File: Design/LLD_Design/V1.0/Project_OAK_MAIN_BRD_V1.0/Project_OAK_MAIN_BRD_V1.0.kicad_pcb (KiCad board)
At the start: 4 copper layers, 41.8 x 46 mm, 109 parts, among them U1 ATmega328PB-MU, U2 RV-8263-C7-32.768KHZ-20PPM-TA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, U3 LIS2DW12TR

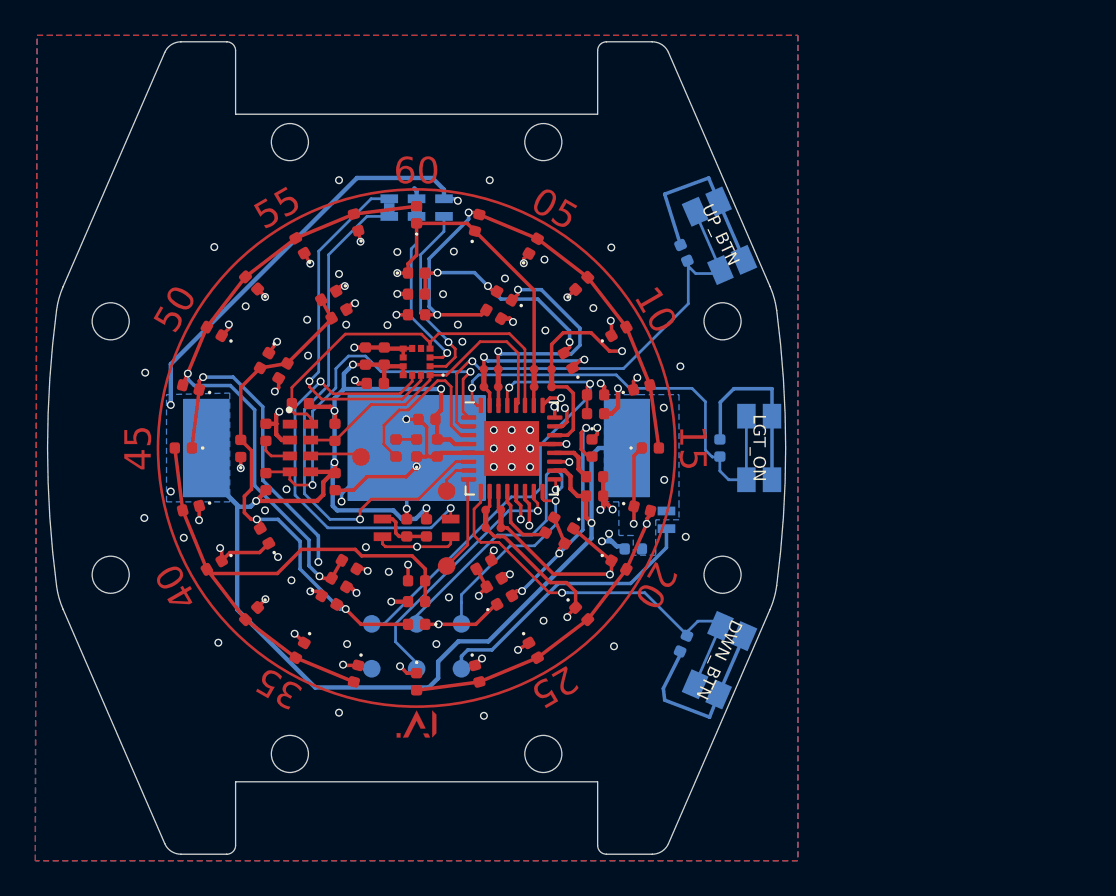
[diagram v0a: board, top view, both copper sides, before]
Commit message: SCH update in progress with ACCL sensor change & haptic sensor addition
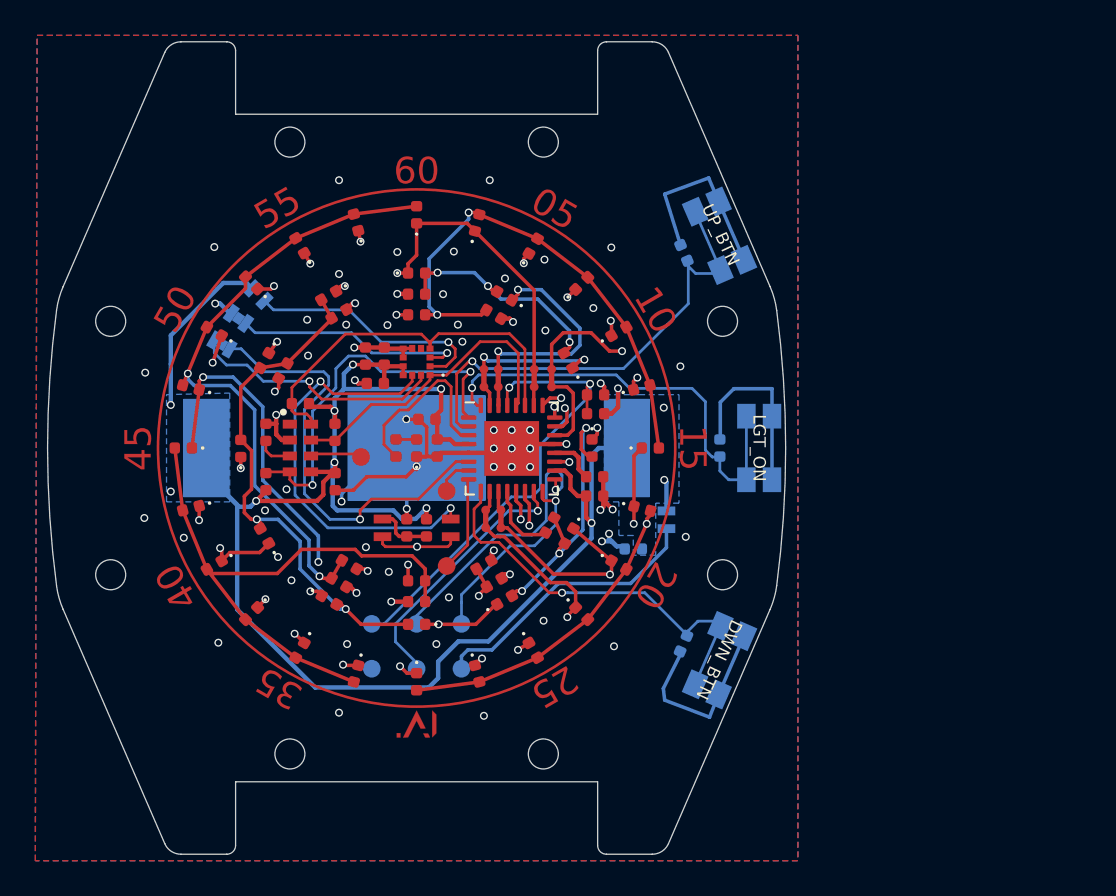
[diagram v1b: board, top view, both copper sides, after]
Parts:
- REF** (x8): footprint MountingHole:MountingHole_2.1mm -> MountingHole:MountingHole_1.7mm
- moved JP5 12.2 mm to (59.4, 87.6), turned to 150 degrees
- moved JP2 11.9 mm to (60.4, 86.1), turned to 325 degrees
- moved JP1 11.6 mm to (61.5, 84.8), turned to 315 degrees
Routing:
- net +3V0: track 123.4 -> 111.4 mm, vias 13 -> 12
- net /ACC_INT1: track 20.5 -> 14.4 mm
- net /PE1: track 30.0 -> 25.0 mm
- net /ACC_SDA0: track 9.78 -> 13.2 mm
- net /ACC_CS: track 11.0 -> 14.1 mm
- net /R5: track 88.5 -> 86.7 mm
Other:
- board text added: "Haptic Sensor"

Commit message: layout update in progress
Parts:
- removed JP1: SolderJumper_2_Open, Jumper:SolderJumper-2_Open_Pad1.0x1.5mm_custom
- removed JP2: SolderJumper_2_Bridged, Jumper:SolderJumper-2_Bridged_Pad1.0x1.5mm_custom
- removed R18, R19, R22, R23, R26: 560E, Resistor_SMD:R_0402_1005Metric
- added C20: 1u, Capacitor_SMD:C_0402_1005Metric, F.Cu at (103.5, 88.1)
- added NT7: Net-Tie_2, NetTie:NetTie-2_SMD_Custom, F.Cu at (61.9, 92.5)
- added R1: 1k, Resistor_SMD:R_0402_1005Metric, F.Cu at (100.8, 90.1)
- added R2: 1k, Resistor_SMD:R_0402_1005Metric, F.Cu at (102.5, 88.1)
- added R3: 100k, Resistor_SMD:R_0402_1005Metric, F.Cu at (101.4, 88.1)
- added R4: 560E, Resistor_SMD:R_0402_1005Metric, F.Cu at (78.1, 97.9)
- added R5: 560E, Resistor_SMD:R_0402_1005Metric, F.Cu at (62.8, 89.1)
- added R8: 560E, Resistor_SMD:R_0402_1005Metric, F.Cu at (74.3, 100.1)
- added R9: 560E, Resistor_SMD:R_0402_1005Metric, F.Cu at (70.5, 101.0)
- added TP2: TestPoint, TestPoint:TestPoint_Pad_D1.0mm, B.Cu at (98.2, 85.7)
- added TP8: TestPoint, TestPoint:TestPoint_Pad_D1.0mm, B.Cu at (98.2, 88.8)
- added U4: DRV2605LYZF, Sensor:DRV2605LYZFR, F.Cu at (102.4, 90.2)
- C11: value 10u -> 1u
- R10, R11: value 10k -> 4.7k
- R7: value 10k -> 560E
- U3: value LIS2DW12TR -> BMA400; footprint Sensor:LIS2DW12TR -> Sensor:BMA400
- moved C11 36.5 mm to (104.0, 90.1)
- moved R7 10.8 mm to (70.5, 85.9), turned to 0 degrees
- moved C10 4.92 mm to (72.4, 87.3), turned to 90 degrees
- moved C5 0.38 mm to (68.6, 87.9), turned to 270 degrees
- moved U3 0.38 mm to (70.5, 88.2)
- moved R13 0.06 mm to (66.6, 100.1)
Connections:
- net /C1_T renamed /LED MATRIX/C1_T
- net /C2_T renamed /LED MATRIX/C2_T
- net /C4_T renamed /LED MATRIX/C4_T
- net /C5_T renamed /LED MATRIX/C5_T
- net /C6_T renamed /LED MATRIX/C6_T
- C16 pad 1: /C3_T -> /LED MATRIX/C3_T
- D10 pad 2: /C3_T -> /LED MATRIX/C3_T
- D16 pad 2: /C3_T -> /LED MATRIX/C3_T
- D22 pad 2: /C3_T -> /LED MATRIX/C3_T
- D28 pad 2: /C3_T -> /LED MATRIX/C3_T
- D34 pad 2: /C3_T -> /LED MATRIX/C3_T
- D4 pad 2: /C3_T -> /LED MATRIX/C3_T
- R7 pad 1: /RTC_CLKO_EN -> /C3
- R7 pad 2: GND -> /LED MATRIX/C3_T
- U3 pad 1: /SNS_SCL -> GND
- U3 pad 11: /ACC_INT2 -> (no net)
- U3 pad 12: /ACC_INT1 -> /SNS_SCL
- U3 pad 2: /ACC_CS -> /SNS_SDA
- U3 pad 3: /ACC_SDA0 -> +3V0
- U3 pad 4: /SNS_SDA -> (no net)
- U3 pad 5: (no net) -> /ACC_INT1
- U3 pad 6: GND -> /ACC_INT2
- U3 pad 7: GND -> +3V0
- U3 pad 9: +3V0 -> GND
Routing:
- net /C3_T: track 29.0 -> 0.00 mm, vias 2 -> 1
- net /LED MATRIX/C3_T: track 0.00 -> 28.0 mm, vias 0 -> 1
- net /ACC_CS: track 14.1 -> 0.00 mm, vias 1 -> 0
- net /ACC_SDA0: track 13.2 -> 0.00 mm, vias 1 -> 0
- net +3V0: track 111.4 -> 104.5 mm
- net /SNS_SCL: track 17.5 -> 13.3 mm
- net GND: track 82.9 -> 78.8 mm, vias 66 -> 61
- net /SNS_SDA: track 22.2 -> 18.4 mm
- net /MON_LED: track 10.5 -> 7.68 mm
- net /ACC_INT2: track 23.8 -> 25.2 mm
- net /RTC_INTO: track 21.6 -> 22.8 mm
- net /ACC_INT1: track 14.4 -> 15.5 mm

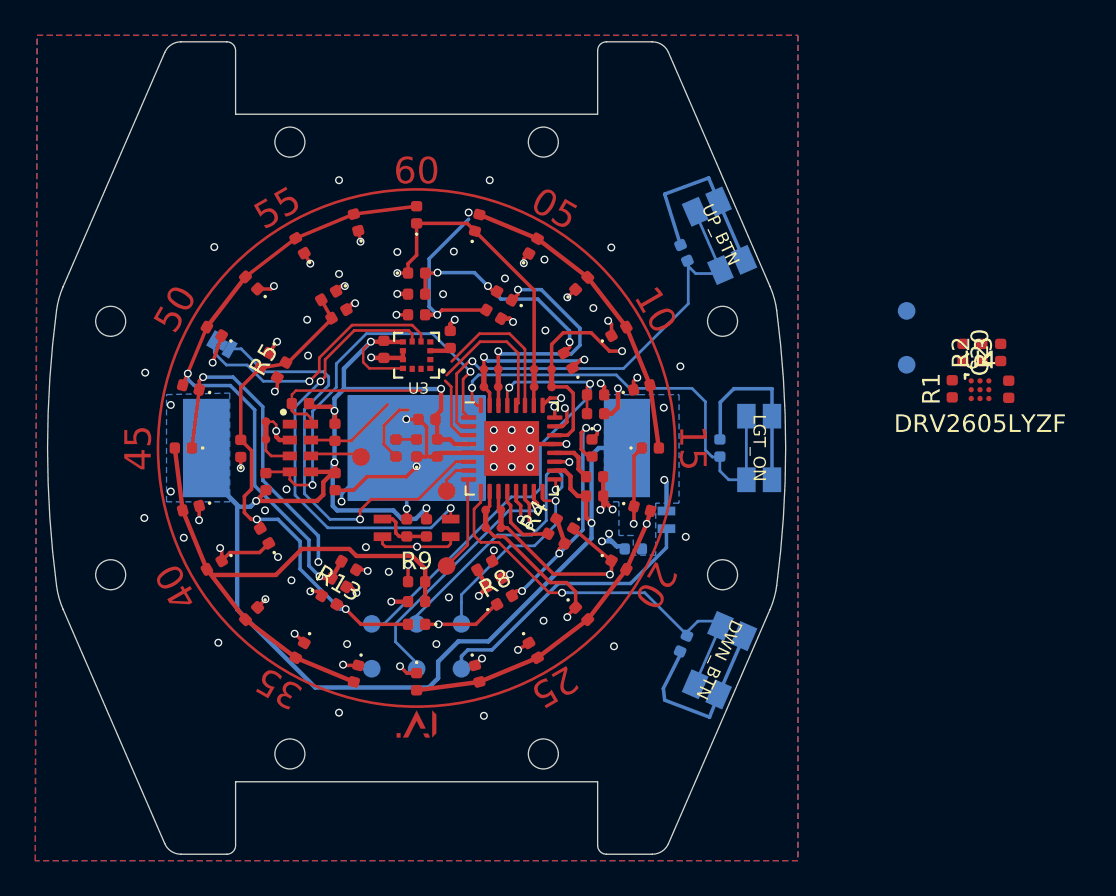
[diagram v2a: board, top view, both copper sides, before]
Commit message: OAK V1.0 main board layout update
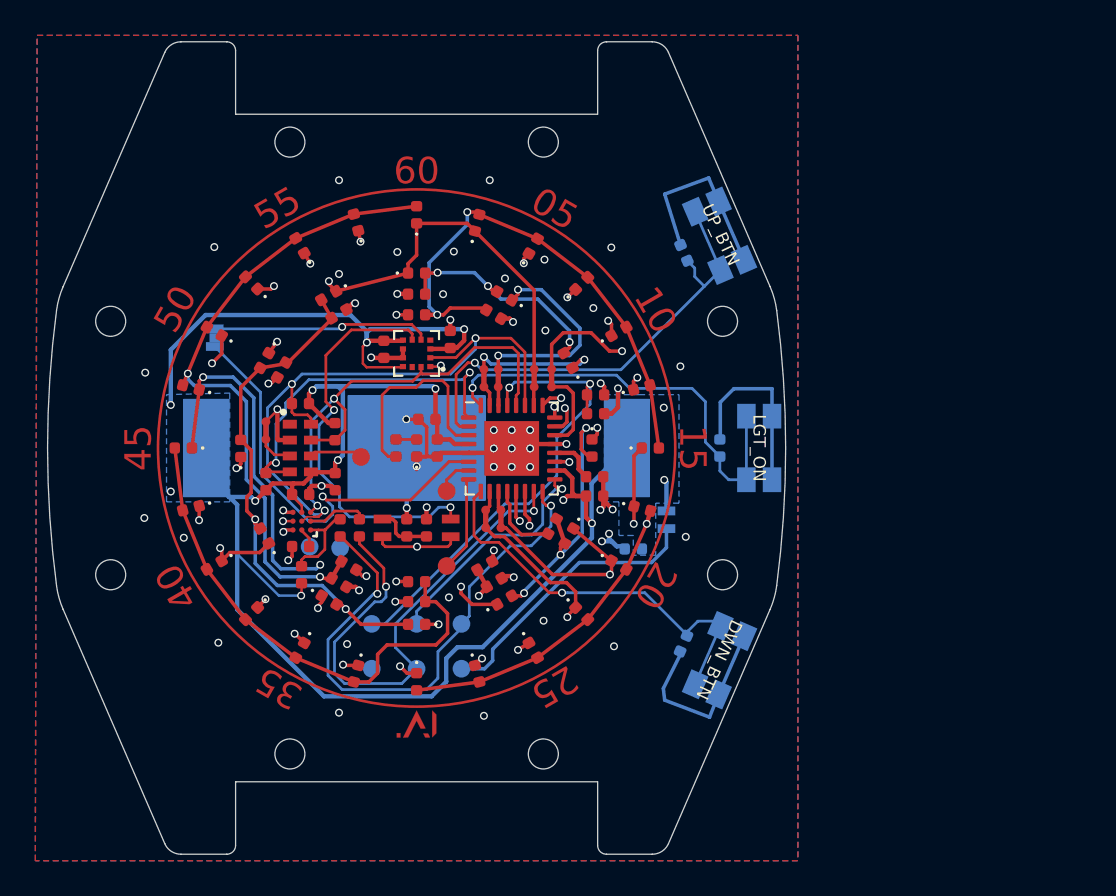
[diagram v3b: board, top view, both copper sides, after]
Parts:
- moved C20 41.1 mm to (63.9, 99.0), turned to 180 degrees
- moved C11 40.5 mm to (63.9, 96.1), turned to 0 degrees
- moved R3 39.5 mm to (63.9, 100.6), turned to 90 degrees
- moved U4 39.1 mm to (64.0, 97.6), turned to 180 degrees
- moved R2 37.7 mm to (66.1, 98.0), turned to 270 degrees
- moved TP8 35.3 mm to (64.4, 99.1)
- moved TP2 34.8 mm to (66.1, 99.1)
- moved R1 34.5 mm to (67.2, 98.0), turned to 270 degrees
- moved JP5 0.56 mm to (59.0, 87.2), turned to 90 degrees
- moved U3 0.10 mm to (70.5, 88.1)
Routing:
- net +3V0: track 104.5 -> 134.0 mm, vias 12 -> 15
- net /ICSP_MISO: track 11.2 -> 31.1 mm, vias 1 -> 2
- net /SNS_SDA: track 18.4 -> 35.6 mm, vias 0 -> 3
- net /ICSP_MOSI: track 14.9 -> 29.7 mm, vias 1 -> 2
- net /SNS_SCL: track 13.3 -> 26.7 mm, vias 0 -> 2
- net GND: track 78.8 -> 73.5 mm, vias 61 -> 55
- net /HAP_EN: track 0.00 -> 4.95 mm
- net /LED MATRIX/C5_T: track 33.5 -> 29.0 mm
- net /MON_LED: track 7.68 -> 11.9 mm
- net /HAP_TRIG: track 0.00 -> 3.39 mm
- net /ACC_INT1: track 15.5 -> 12.3 mm
- net /R6: track 74.4 -> 77.5 mm, vias 5 -> 6
- net /RTC_INTO: track 22.8 -> 19.9 mm
- net /C3: track 34.4 -> 36.9 mm
- net /C2: track 23.6 -> 25.9 mm
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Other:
- net class bga added: clearance 0.05, trace_width 0.1565, via_dia 0.45, via_drill 0.3

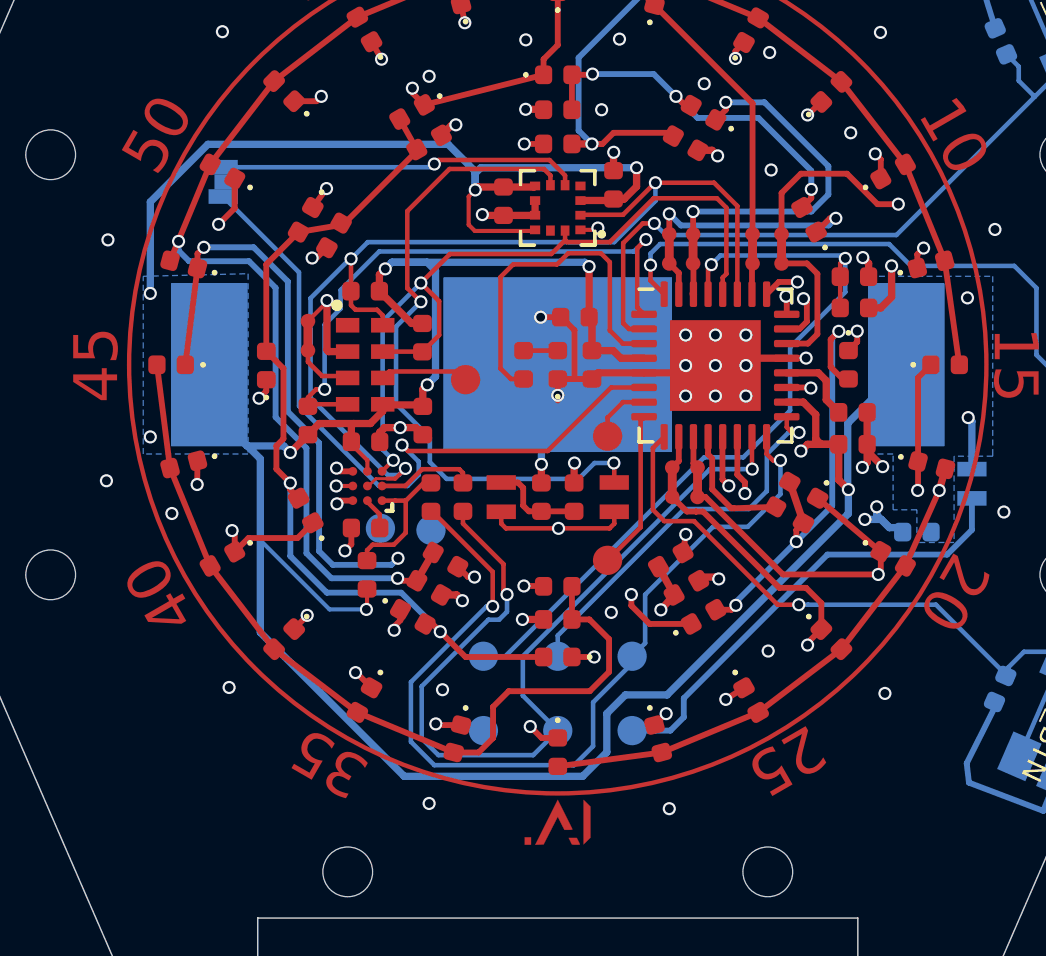
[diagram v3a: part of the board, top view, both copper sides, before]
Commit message: OAK V1.0 main board routing complete
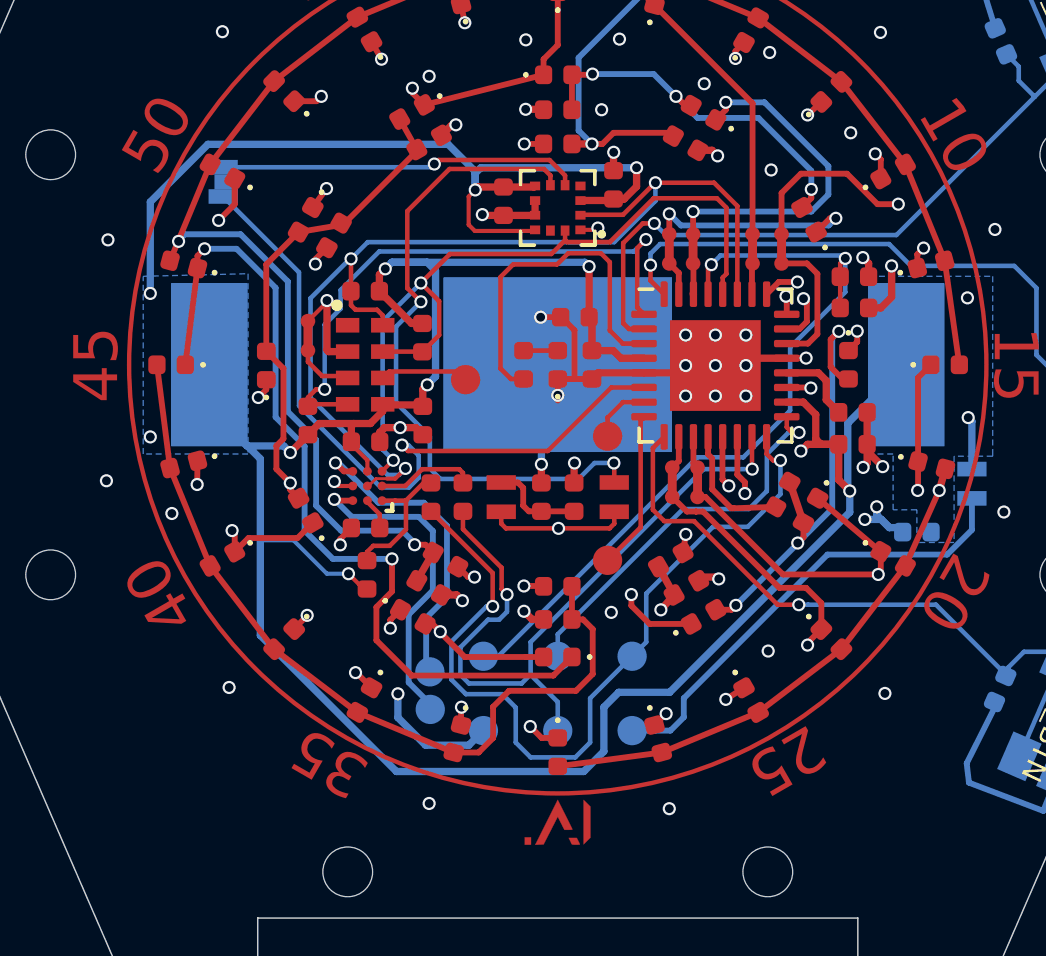
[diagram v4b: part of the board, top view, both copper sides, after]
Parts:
- moved TP8 6.41 mm to (66.1, 105.2)
- moved TP2 4.84 mm to (66.1, 104.0)
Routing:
- net /HAP_DRV_POS: track 0.59 -> 11.2 mm
- net /HAP_DRV_NEG: track 0.60 -> 10.8 mm
- net /ICSP_MOSI: track 29.7 -> 24.3 mm
- net GND: track 73.5 -> 77.9 mm
- net /R6: track 77.5 -> 74.3 mm, vias 6 -> 5
- net /ICSP_MISO: track 31.1 -> 28.3 mm
- net /R1: track 52.0 -> 51.0 mm
- net /LED MATRIX/C5_T: track 29.0 -> 28.1 mm
- net /LED MATRIX/C6_T: track 36.8 -> 36.2 mm

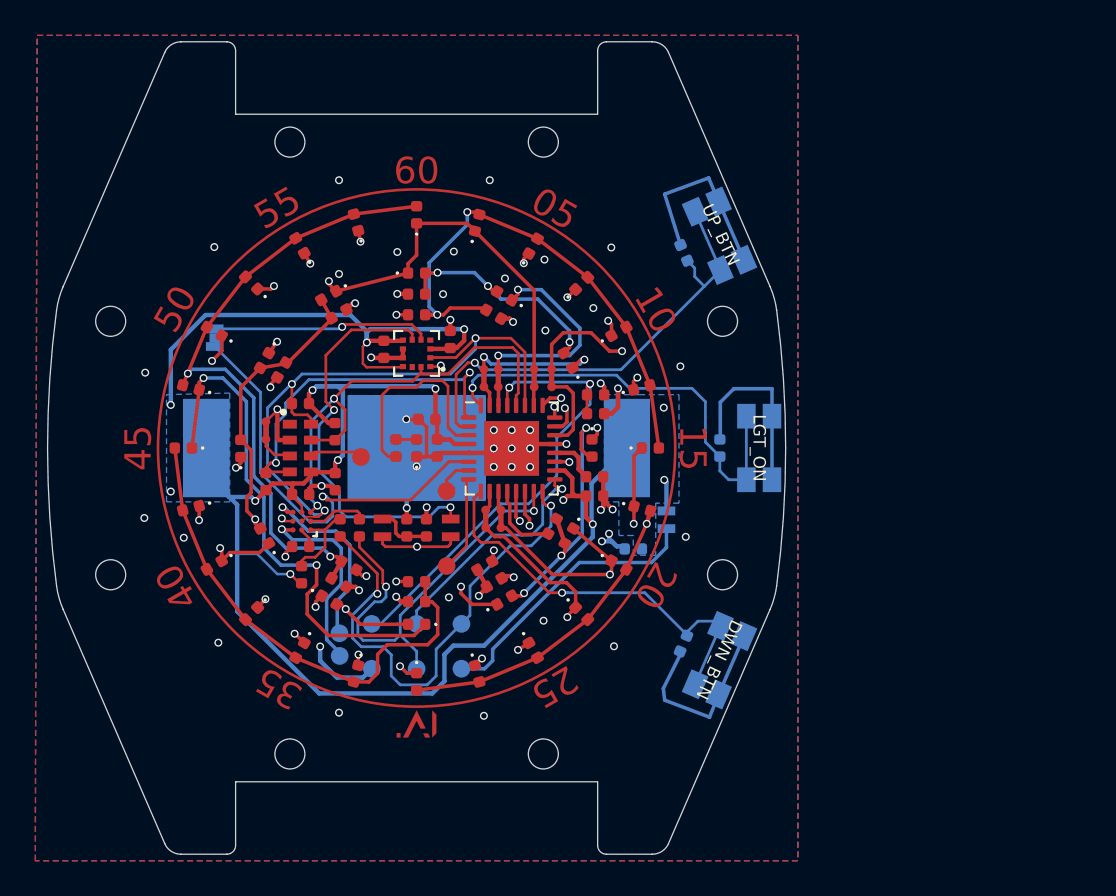
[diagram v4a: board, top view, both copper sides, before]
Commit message: updated PCB and Gerber with final mechanical fitment
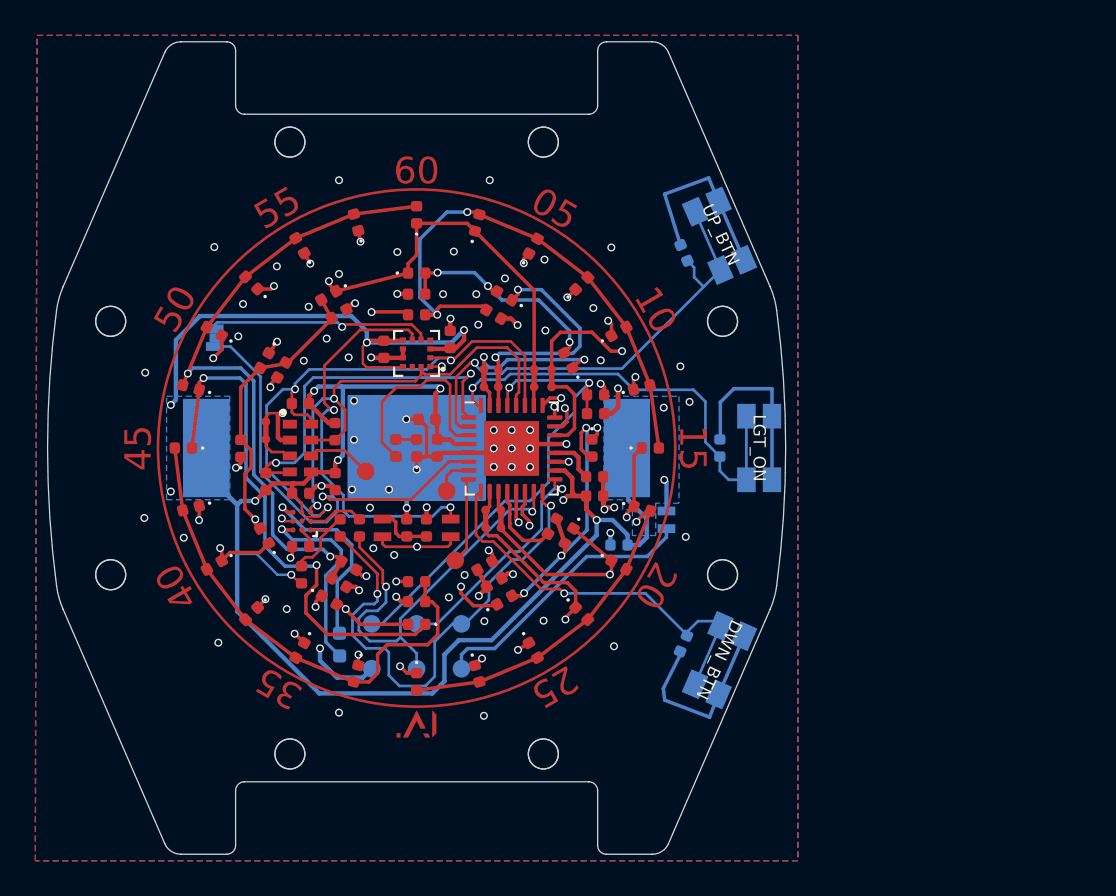
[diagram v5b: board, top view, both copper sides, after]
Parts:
- moved TP11 0.86 mm to (67.6, 94.8)
- moved C4 0.84 mm to (81.9, 99.0)
- moved TP7 0.58 mm to (72.6, 99.8)
- moved C11 0.06 mm to (63.9, 96.0)
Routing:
- net +3V0: track 133.8 -> 137.3 mm
- net /R5: track 86.3 -> 88.9 mm
- net /SNS_SDA: track 35.6 -> 34.0 mm
- net /LED MATRIX/C3_T: track 29.2 -> 30.6 mm
- net /LED MATRIX/C4_T: track 31.2 -> 32.3 mm
- net GND: track 77.9 -> 76.8 mm, vias 55 -> 75
- net /PE1: track 24.3 -> 25.2 mm
- net /SNS_SCL: track 26.7 -> 27.4 mm
- net /C3: track 36.6 -> 37.3 mm
- net /RTC_CLKO: track 3.04 -> 3.71 mm
- net /RTC_INTO: track 19.9 -> 20.5 mm
- net /LED MATRIX/C6_T: track 36.2 -> 36.8 mm
- net /PB7: track 5.42 -> 4.90 mm
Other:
- outline, holes or cut-outs redrawn
- board text added: "di"
- board text added: "do"
- board text removed: "si"
- board text removed: "so"
